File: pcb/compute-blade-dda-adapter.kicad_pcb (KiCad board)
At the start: 2 copper layers, 18 x 19.5 mm, 2 parts, among them J1 COMPUTE BLADE, J2 DDA GPS/RTC

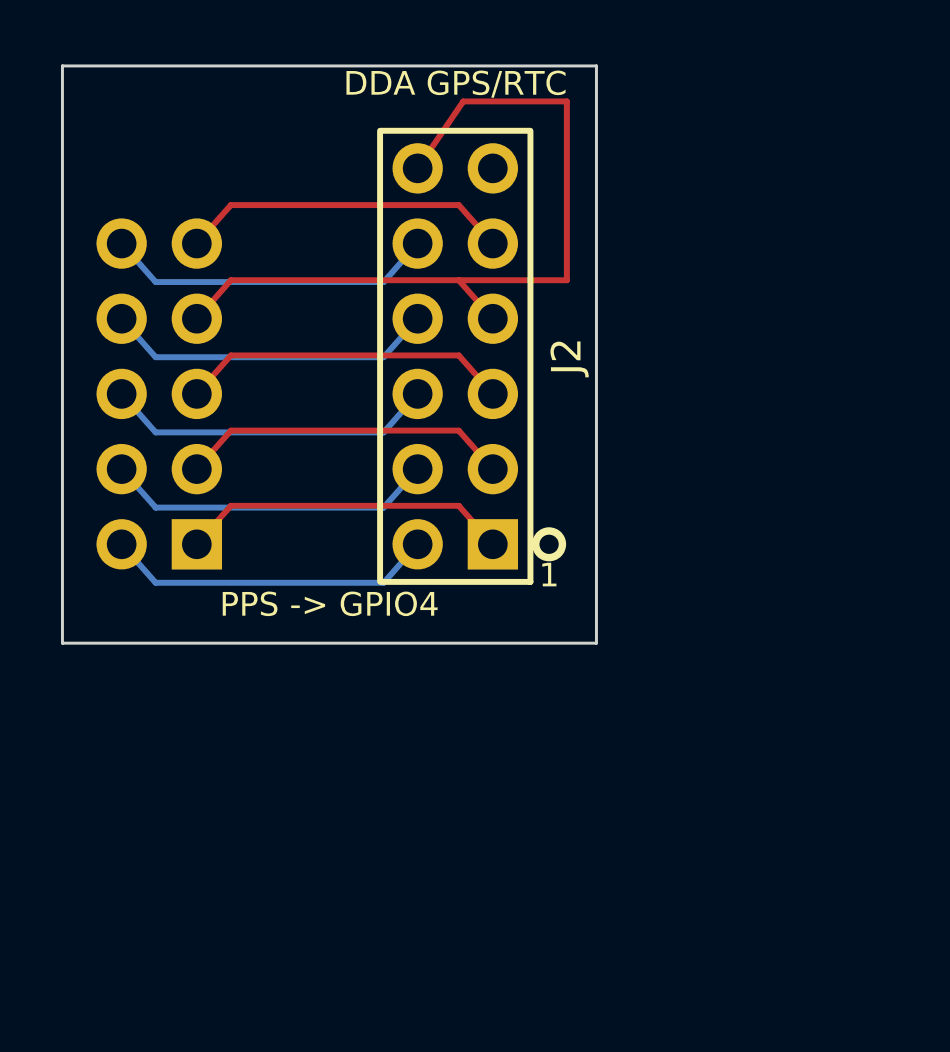
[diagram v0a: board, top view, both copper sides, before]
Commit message: Add upright DDA mechanical revision
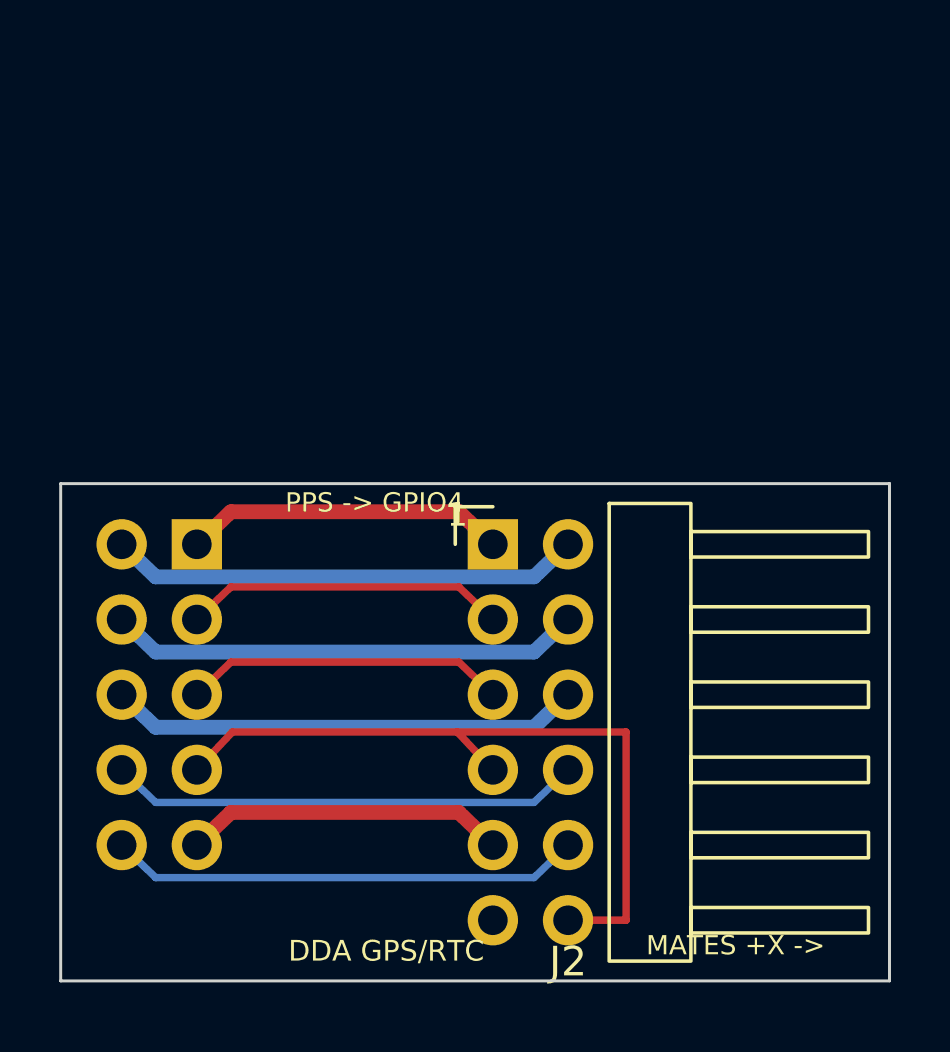
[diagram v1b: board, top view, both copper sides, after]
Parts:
- J2: value DDA GPS/RTC -> DDA GPS/RTC RIGHT-ANGLE; footprint Connector_PinHeader_2.54mm:PinHeader_2x06_P2.54mm_Vertical -> Connector_PinHeader_2.54mm:PinHeader_2x06_P2.54mm_Horizontal
- turned J1 to 0 degrees
- turned J2 to 0 degrees
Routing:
- net UART_RX_FROM_GPS_TX: track 11.2 -> 16.0 mm
- net GND_PIN6: track 11.2 -> 16.0 mm
- net 5V_PIN2: track 11.2 -> 16.0 mm
- net UART_TX_TO_GPS_RX: track 11.2 -> 16.0 mm
- net 5V_PIN4: track 11.2 -> 16.0 mm
- net PPS_GPIO4: track 27.1 -> 25.1 mm
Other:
- board size 18 x 19.5 mm -> 28 x 16.8 mm
